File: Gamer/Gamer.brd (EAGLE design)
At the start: 162 x 64 mm, 53 parts, among them J1 AVR_SPI_PRG_6NS, J2 AVR_SPI_PRG_6NS, J3 AVR_SPI_PRG_6NS, J4 AVR_SPI_PRG_6NS

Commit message: gamer - Starting complete redo of Gamer
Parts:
- removed C10, C11, C8, C9: (no value), resistor:C0603
- removed C6: 0.05uF, resistor:C0603
- removed C7: 1uF, resistor:C0603
- removed J4: AVR_SPI_PRG_6NS, SparkFun-Connectors:2X3-NS
- removed PI-HEADER: (no value), pinhead:2X13
- removed R4: Bypass, resistor:R0603
- removed R5, R6, R8, R9: 100K, resistor:R0603
- removed R7: 10, resistor:R0603
- removed U$1, U$13, U$3, U$8: 8X8_LED_MATRIX, ScottSilver:8X8_LED_MATRIX
- removed U$10, U$14, U$4, U$5: ULN2803AFWG, ScottSilver:ULN2803AFWG
- removed U$11, U$15, U$6, U$9: ATTINY48, ScottSilver:ATTINY48
- removed U$12, U$16, U$2, U$7: RES_ARRAY, ScottSilver:RES_ARRAY
- removed U$17, U$18, U$19, U$20, U$21, U$22: 12X12MM_BUTTON, ScottSilver:12X12MM_BUTTON
- removed U$23: MMA8653FCR1, ScottSilver:MMA8653FCR1
- removed U$24, U$26: SMDTACTILE, ScottSilver:SMDTACTILE
- removed U$25: LM386, ScottSilver:LM386
- removed U$29: DF3_1X2, ScottSilver:DF3_1X2
- removed U$30: DF3_1X5, ScottSilver:DF3_1X5
- added A, B, DOWN, LEFT, RIGHT, UP: 12X12MM_BUTTON, Gamer:12X12MM_BUTTON
- added P1: (no value), HeaderConnectorBoard:2X20
- added P2: NONE, LED_Matrix:1X06
- added PROG: NONE, LED_Matrix:2X03
- added SELECT, START: 6X6MM_BUTTON, Gamer:6X6MM_BUTTON
- added U1: MMA8653FCR1, AccelBreakout:MMA8653FCR1
- added U2: ATTINY48, LED_Matrix:ATTINY48
- added U3: ULN2803AFWG, LED_Matrix:ULN2803AFWG
- C1, C2, C3, C4: device resistor:C0603 -> AccelBreakout:C0603
- C5: value (none) -> 1uF; device resistor:153CLV-0605 -> resistor:C0603
- J1: value AVR_SPI_PRG_6NS -> NONE; device SparkFun-Connectors:2X3-NS -> LED_Matrix:1X06
- J2, J3: value AVR_SPI_PRG_6NS -> HEADER-1X8; device SparkFun-Connectors:2X3-NS -> LED_Matrix:HEADER-1X8
- R1, R2: value 1k -> 10K; device resistor:R0603 -> AccelBreakout:R0603
- R3: value Bypass -> 10k
- moved J2 63.8 mm to (54.1, 28.7), turned to 0 degrees
- moved C5 62.6 mm to (63.5, 38.1), turned to 0 degrees
- moved J3 49.6 mm to (56.6, 61.7), turned to 0 degrees
- moved C4 40.1 mm to (115.3, 31.8), turned to 270 degrees
- moved J1 38.0 mm to (77.7, 40.4), turned to 0 degrees
- moved C3 35.0 mm to (112.5, 29.0), turned to 0 degrees
- moved R2 30.7 mm to (112.5, 34.3)
- moved R1 30.6 mm to (108.2, 34.8), turned to 180 degrees
- moved C2 27.7 mm to (109.5, 31.8), turned to 270 degrees
- moved C1 23.4 mm to (107.4, 31.8), turned to 270 degrees
- moved R3 8.46 mm to (56.4, 37.1), flipped to the top, turned to 0 degrees
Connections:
- removed net A: PI-HEADER.7, U$22.3
- removed net AUDIO: U$25.3, U$30.1
- removed net B: PI-HEADER.11, U$21.3
- removed net DOWN: PI-HEADER.18, U$20.2
- removed net LEFT: PI-HEADER.16, U$18.2
- removed net MISO1/MOSI2: J1.1, J2.4, R3.1, U$6.PB3, U$9.PB4
- removed net MISO2/MOSI3: J2.1, J4.4, R4.1, U$15.PB3, U$6.PB4
- removed net MISO3/MOSI4: J3.4, J4.1, U$11.PB3, U$15.PB4
- removed net N$1: U$1.COL0, U$5.O1
- removed net N$10: U$1.ROW6, U$2.2R
- removed net N$100: U$11.PC4, U$12.R2
- removed net N$101: U$11.PC5, U$12.R1
- removed net N$102: U$15.PC7, U$16.R8
- removed net N$103: U$13.COL0, U$14.O1
- removed net N$104: U$13.COL1, U$14.O2
- removed net N$105: U$13.COL2, U$14.O3
- removed net N$106: U$13.COL3, U$14.O4
- removed net N$107: U$13.COL4, U$14.O5
- removed net N$108: U$13.COL5, U$14.O6
- removed net N$109: U$13.COL6, U$14.O7
- removed net N$11: U$1.ROW5, U$2.3R
- removed net N$110: U$13.COL7, U$14.O8
- removed net N$111: U$13.ROW7, U$16.1R
- removed net N$112: U$13.ROW6, U$16.2R
- removed net N$113: U$13.ROW5, U$16.3R
- removed net N$114: U$13.ROW4, U$16.4R
- removed net N$115: U$13.ROW3, U$16.5R
- removed net N$116: U$13.ROW2, U$16.6R
- removed net N$117: U$13.ROW1, U$16.7R
- removed net N$118: U$13.ROW0, U$16.8R
- removed net N$119: U$14.I1, U$15.PD0
- removed net N$12: U$1.ROW4, U$2.4R
- removed net N$120: U$14.I2, U$15.PD1
- removed net N$121: U$14.I3, U$15.PD2
- removed net N$122: U$14.I4, U$15.PD3
- removed net N$123: U$14.I5, U$15.PD4
- removed net N$124: U$14.I6, U$15.PD5
- removed net N$125: U$14.I7, U$15.PD6
- removed net N$126: U$14.I8, U$15.PD7
- removed net N$129: U$15.PC0, U$16.R6
- removed net N$13: U$1.ROW3, U$2.5R
- removed net N$130: U$15.PC1, U$16.R5
- removed net N$131: U$15.PC2, U$16.R4
- removed net N$132: U$15.PC3, U$16.R3
- removed net N$133: U$15.PC4, U$16.R2
- removed net N$134: U$15.PC5, U$16.R1
- removed net N$14: U$1.ROW2, U$2.6R
- removed net N$15: U$1.ROW1, U$2.7R
- removed net N$16: U$1.ROW0, U$2.8R
- removed net N$17: U$5.I1, U$9.PD0
- removed net N$18: U$5.I2, U$9.PD1
- removed net N$19: U$5.I3, U$9.PD2
- removed net N$2: U$1.COL1, U$5.O2
- removed net N$20: U$5.I4, U$9.PD3
- removed net N$21: U$5.I5, U$9.PD4
- removed net N$22: U$5.I6, U$9.PD5
- removed net N$23: U$5.I7, U$9.PD6
- removed net N$24: U$5.I8, U$9.PD7
- removed net N$25: U$2.R7, U$9.PA1
- removed net N$26: U$2.R8, U$9.PC7
- removed net N$27: U$2.R6, U$9.PC0
- removed net N$28: U$2.R5, U$9.PC1
- removed net N$29: U$2.R4, U$9.PC2
- removed net N$3: U$1.COL2, U$5.O3
- removed net N$30: U$2.R3, U$9.PC3
- removed net N$31: U$2.R2, U$9.PC4
- removed net N$32: U$2.R1, U$9.PC5
- removed net N$33: C7.1, U$25.7
- removed net N$35: C5.+, C6.1, U$25.5
- removed net N$36: U$3.COL0, U$4.O1
- removed net N$37: C6.2, R7.2
- removed net N$38: U$3.COL1, U$4.O2
- removed net N$39: U$3.COL2, U$4.O3
- removed net N$4: U$1.COL3, U$5.O4
- removed net N$40: U$3.COL3, U$4.O4
- removed net N$41: U$3.COL4, U$4.O5
- removed net N$42: U$3.COL5, U$4.O6
- removed net N$43: U$3.COL6, U$4.O7
- removed net N$44: U$3.COL7, U$4.O8
- removed net N$45: U$3.ROW7, U$7.1R
- removed net N$46: U$3.ROW6, U$7.2R
- removed net N$47: U$3.ROW5, U$7.3R
- removed net N$48: U$3.ROW4, U$7.4R
- removed net N$49: U$3.ROW3, U$7.5R
- removed net N$5: U$1.COL4, U$5.O5
- removed net N$50: U$3.ROW2, U$7.6R
- removed net N$51: U$3.ROW1, U$7.7R
- removed net N$52: U$3.ROW0, U$7.8R
- removed net N$53: U$4.I1, U$6.PD0
- removed net N$54: U$4.I2, U$6.PD1
- removed net N$55: U$4.I3, U$6.PD2
- removed net N$56: U$4.I4, U$6.PD3
- removed net N$57: U$4.I5, U$6.PD4
- removed net N$58: U$4.I6, U$6.PD5
- removed net N$59: U$4.I7, U$6.PD6
- removed net N$6: U$1.COL5, U$5.O6
- removed net N$60: U$4.I8, U$6.PD7
- removed net N$61: U$6.PA1, U$7.R7
- removed net N$62: U$6.PC7, U$7.R8
- removed net N$63: U$6.PC0, U$7.R6
- removed net N$64: U$6.PC1, U$7.R5
- removed net N$65: U$6.PC2, U$7.R4
- removed net N$66: U$6.PC3, U$7.R3
- removed net N$67: U$6.PC4, U$7.R2
- removed net N$68: U$6.PC5, U$7.R1
- removed net N$69: U$15.PA1, U$16.R7
- removed net N$7: U$1.COL6, U$5.O7
- removed net N$70: U$10.O1, U$8.COL0
- removed net N$71: U$10.O2, U$8.COL1
- removed net N$72: U$10.O3, U$8.COL2
- removed net N$73: U$10.O4, U$8.COL3
- removed net N$74: U$10.O5, U$8.COL4
- removed net N$75: U$10.O6, U$8.COL5
- removed net N$76: U$10.O7, U$8.COL6
- removed net N$77: U$10.O8, U$8.COL7
- removed net N$78: U$12.1R, U$8.ROW7
- removed net N$79: U$12.2R, U$8.ROW6
- removed net N$8: U$1.COL7, U$5.O8
- removed net N$80: U$12.3R, U$8.ROW5
- removed net N$81: U$12.4R, U$8.ROW4
- removed net N$82: U$12.5R, U$8.ROW3
- removed net N$83: U$12.6R, U$8.ROW2
- removed net N$84: U$12.7R, U$8.ROW1
- removed net N$85: U$12.8R, U$8.ROW0
- removed net N$86: U$10.I1, U$11.PD0
- removed net N$87: U$10.I2, U$11.PD1
- removed net N$88: U$10.I3, U$11.PD2
- removed net N$89: U$10.I4, U$11.PD3
- removed net N$9: U$1.ROW7, U$2.1R
- removed net N$90: U$10.I5, U$11.PD4
- removed net N$91: U$10.I6, U$11.PD5
- removed net N$92: U$10.I7, U$11.PD6
- removed net N$93: U$10.I8, U$11.PD7
- removed net N$94: U$11.PA1, U$12.R7
- removed net N$95: U$11.PC7, U$12.R8
- removed net N$96: U$11.PC0, U$12.R6
- removed net N$97: U$11.PC1, U$12.R5
- removed net N$98: U$11.PC2, U$12.R4
- removed net N$99: U$11.PC3, U$12.R3
- removed net RIGHT: PI-HEADER.12, U$19.2
- removed net SELECT: PI-HEADER.15, U$26.1
- removed net SPK: C5.-, U$29.1
- removed net SS: PI-HEADER.24, U$11.PB2, U$15.PB2, U$6.PB2, U$9.PB2
- removed net START: PI-HEADER.13, U$24.1
- removed net UP: PI-HEADER.22, U$17.2
- new net 10/MOSI: P1.19
- new net 11/CLK: P1.23
- new net 12: P1.32
- new net 13: P1.33
- new net 14/TX: P1.8
- new net 15/RX: P1.10
- new net 16: P1.36
- new net 17/RTS: B.3, P1.11
- new net 18: P1.12, RIGHT.2
- new net 19: P1.35
- new net 2/SDA: P1.3
- new net 20: P1.38
- new net 21: P1.40
- new net 22: P1.15, SELECT.2
- new net 23: LEFT.2, P1.16
- new net 24: DOWN.2, P1.18
- new net 25: P1.22, UP.2
- new net 26: P1.37
- new net 27: P1.13, START.2
- new net 3.3V_1: P1.1
- new net 3.3V_2: P1.17
- new net 3/SCL: P1.5
- new net 4: A.3, P1.7
- new net 5: P1.29
- new net 5V_1: P1.4
- new net 5V_2: P1.2
- new net 6: P1.31
- new net 7/CE1: P1.26
- new net 8/CE0: P1.24
- new net 9/MISO: P1.21
- new net COL0: J3.8, U3.O1
- new net COL0_SINK: U2.PD0, U3.I1
- new net COL1: J3.7, U3.O2
- new net COL1_SINK: U2.PD1, U3.I2
- new net COL2: J3.3, U3.O3
- new net COL2_SINK: U2.PD2, U3.I3
- new net COL3: J2.3, U3.O4
- new net COL3_SINK: U2.PD3, U3.I4
- new net COL4: J3.2, U3.O5
- new net COL4_SINK: U2.PD4, U3.I5
- new net COL5: J2.5, U3.O6
- new net COL5_SINK: U2.PD5, U3.I6
- new net COL6: J2.6, U3.O7
- new net COL6_SINK: U2.PD6, U3.I7
- new net COL7: J3.5, U3.O8
- new net COL7_SINK: U2.PD7, U3.I8
- new net CS: J1.4, P2.4, U2.PB2
- new net GND2: P1.25
- new net GND3: P1.20
- new net GND4: P1.14
- new net GND5: P1.6
- new net GND6: P1.39
- new net GND7: P1.34
- new net GND8: P1.30
- new net ID1: P1.27
- new net ID2: P1.28
- new net ROW0: J3.1, U2.PC7
- new net ROW1: J3.6, U2.PA1
- new net ROW2: J2.1, U2.PC0
- new net ROW3: J3.4, U2.PC1
- new net ROW4: J2.8, U2.PC2
- new net ROW5: J2.2, U2.PC3
- new net ROW6: J2.7, U2.PC4
- new net ROW7: J2.4, U2.PC5
- net GND: now also A.1, B.1, C5.2, DOWN.4, LEFT.4, P1.9, P2.6, PROG.2, RIGHT.4, SELECT.4, START.4, U1.6, U1.7, U1.9, U2.AGND, U2.GND, U3.GND, UP.4; no longer C10.2, C11.2, C7.2, C8.2, C9.2, J2.6, J3.6, J4.6, PI-HEADER.6, R7.1, U$10.GND, U$11.AGND, U$11.GND, U$14.GND, U$15.AGND, U$15.GND, U$17.4, U$18.4, U$19.4, U$20.4, U$21.1, U$22.1, U$23.6, U$23.7, U$23.9, U$24.4, U$25.2, U$25.4, U$26.4, U$29.2, U$30.2, U$30.5, U$4.GND, U$5.GND, U$6.AGND, U$6.GND, U$9.AGND, U$9.GND
- net INT1: now also U1.3; no longer PI-HEADER.10, U$23.3
- net INT2: now also U1.5; no longer PI-HEADER.8, U$23.5
- net MISO: now also J1.3, PROG.5, U2.PB4; no longer J3.1, PI-HEADER.21, R3.2, R4.2, U$11.PB4
- net MOSI: now also P2.3, PROG.4, U2.PB3; no longer J1.4, PI-HEADER.19, U$9.PB3
- net N$34: now also U1.4; no longer U$23.4
- net RESET: now also P2.5, PROG.1, R3.2, U2.PC6; no longer J2.5, J3.5, J4.5, R5.1, R6.1, R8.1, R9.1, U$11.PC6, U$15.PC6, U$6.PC6, U$9.PC6
- net SCK: now also J1.2, P2.2, PROG.3, U2.PB5; no longer J1.3, J2.3, J3.3, J4.3, PI-HEADER.23, U$11.PB5, U$15.PB5, U$6.PB5, U$9.PB5
- net SCL: now also R1.1, U1.2; no longer PI-HEADER.5, R2.2, U$23.2
- net SDA: now also R2.1, U1.10; no longer PI-HEADER.3, R1.1, U$23.10
- net VCC: now also C5.1, J1.1, P2.1, PROG.6, R2.2, R3.1, U1.1, U1.8, U2.AVCC, U2.VCC, U3.COMMON; no longer C10.1, C11.1, C8.1, C9.1, J1.2, J2.2, J3.2, J4.2, R2.1, R5.2, R6.2, R8.2, R9.2, U$10.COMMON, U$11.AVCC, U$11.VCC, U$14.COMMON, U$15.AVCC, U$15.VCC, U$23.1, U$23.8, U$25.6, U$30.4, U$4.COMMON, U$5.COMMON, U$6.AVCC, U$6.VCC, U$9.AVCC, U$9.VCC
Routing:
- net GND: track 509.6 -> 0.00 mm, vias 20 -> 0
- net VCC: track 321.8 -> 0.00 mm, vias 12 -> 0
- net SCK: track 266.7 -> 0.00 mm, vias 6 -> 0
- net RESET: track 240.3 -> 0.00 mm, vias 3 -> 0
- net UP: track 199.5 -> 0.00 mm, vias 1 -> 0
- net LEFT: track 169.2 -> 0.00 mm, vias 1 -> 0
- net MISO: track 162.3 -> 0.00 mm, vias 3 -> 0
- net SS: track 156.7 -> 0.00 mm, vias 6 -> 0
- net MOSI: track 152.5 -> 0.00 mm, vias 1 -> 0
- net DOWN: track 151.5 -> 0.00 mm, vias 2 -> 0
- net RIGHT: track 142.0 -> 0.00 mm, vias 4 -> 0
- net START: track 124.9 -> 0.00 mm, vias 3 -> 0
- net SELECT: track 116.5 -> 0.00 mm, vias 3 -> 0
- net MISO3/MOSI4: track 104.7 -> 0.00 mm, vias 2 -> 0
- net MISO1/MOSI2: track 99.5 -> 0.00 mm, vias 3 -> 0
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- removed copper zone on layer 16, net GND
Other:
- board size 162 x 64 mm -> 168.9 x 63.5 mm
- board text removed: "B1"
- board text removed: "B2"
- board text removed: "B3"
- board text removed: "B4"
- board text removed: "B5"
- board text removed: "B6"
- board text removed: "B7"
- board text removed: "B8"
- board text removed: "GND"
- board text removed: "J1"
- board text removed: "J10"
- board text removed: "J11"
- board text removed: "J12"
- board text removed: "J13"
- board text removed: "J14"
- board text removed: "J15"
- board text removed: "J3"
- board text removed: "J4"
- board text removed: "J5"
- board text removed: "J6"
- board text removed: "J7"
- board text removed: "J8"
- board text removed: "J9"
- board text removed: "MISO"
- board text removed: "MOSI"
- board text removed: "RESET"
- board text removed: "SCK"
- board text removed: "U1"
- board text removed: "U2"
- board text removed: "U3"
- board text removed: "U4"
- board text removed: "U5"
- board text removed: "U6"
- board text removed: "U7"
- board text removed: "U8"
- board text removed: "VCC"

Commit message: gamer - Work in progress
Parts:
- removed J1, P2: NONE, LED_Matrix:1X06
- moved SELECT 79.9 mm to (35.6, 57.8), turned to 90 degrees
- moved START 69.0 mm to (27.9, 57.8), turned to 90 degrees
- moved J2 31.0 mm to (56.5, 59.6)
- moved J3 26.1 mm to (56.5, 35.6)
- moved R3 19.7 mm to (69.8, 51.4)
- moved PROG 16.5 mm to (72.6, 57.1), flipped to the bottom
- moved U3 13.6 mm to (53.4, 52.7), turned to 180 degrees
- moved C5 10.9 mm to (69.8, 47.0)
- moved U2 3.70 mm to (61.3, 47.9)
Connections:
- removed net 11/CLK: P1.23
- removed net CS: J1.4, P2.4, U2.PB2
- removed net MISO: J1.3, PROG.5, U2.PB4
- removed net SCK: J1.2, P2.2, PROG.3, U2.PB5
- new net 11/SCLK: P1.23, PROG.3, U2.PB5
- net 8/CE0: now also U2.PB2
- net 9/MISO: now also PROG.5, U2.PB4
- net GND: no longer J1.6, P2.6
- net MOSI: no longer P2.3
- net RESET: no longer J1.5, P2.5
- net VCC: no longer J1.1, P2.1

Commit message: gamer - Duplicated matrices (not laid out)
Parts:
- added C6, C7, C8: 1uF, resistor:C0603
- added J1, J4, J5, J6, J7, J8: HEADER-1X8, LED_Matrix:HEADER-1X8
- added PROG1, PROG2, PROG3: NONE, LED_Matrix:2X03
- added R4, R5, R6: 10k, resistor:R0603
- added U4, U6, U8: ATTINY48, LED_Matrix:ATTINY48
- added U5, U7, U9: ULN2803AFWG, LED_Matrix:ULN2803AFWG
- moved J3 76.2 mm to (10.8, -25.4)
- moved PROG 42.6 mm to (115.2, 58.4), flipped to the top, turned to 270 degrees
- moved J2 24.0 mm to (56.5, 35.6)
- moved P1 2.54 mm to (134.6, 45.7)
- moved U3 1.30 mm to (52.1, 52.7)
- moved A 1.27 mm to (129.5, 16.5)
- moved B 1.27 mm to (143.5, 30.5)
- moved U2 0.54 mm to (61.0, 48.3)
- turned C5 to 90 degrees
- turned R3 to 90 degrees
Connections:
- net COL0_SINK renamed M1_COL0_SINK
- net COL1_SINK renamed M1_COL1_SINK
- net COL2_SINK renamed M1_COL2_SINK
- net COL3_SINK renamed M1_COL3_SINK
- net COL4_SINK renamed M1_COL4_SINK
- net COL5_SINK renamed M1_COL5_SINK
- net COL6_SINK renamed M1_COL6_SINK
- net COL7_SINK renamed M1_COL7_SINK
- net RESET renamed M1_RESET
- removed net COL0: J3.8, U3.O1
- removed net COL1: J3.7, U3.O2
- removed net COL2: J3.3, U3.O3
- removed net COL3: J2.3, U3.O4
- removed net COL4: J3.2, U3.O5
- removed net COL5: J2.5, U3.O6
- removed net COL6: J2.6, U3.O7
- removed net COL7: J3.5, U3.O8
- removed net MOSI: PROG.4, U2.PB3
- removed net ROW0: J3.1, U2.PC7
- removed net ROW1: J3.6, U2.PA1
- removed net ROW2: J2.1, U2.PC0
- removed net ROW3: J3.4, U2.PC1
- removed net ROW4: J2.8, U2.PC2
- removed net ROW5: J2.2, U2.PC3
- removed net ROW6: J2.7, U2.PC4
- removed net ROW7: J2.4, U2.PC5
- new net M1_COL0: J2.8, U3.O1
- new net M1_COL1: J2.7, U3.O2
- new net M1_COL2: J2.3, U3.O3
- new net M1_COL3: J1.3, U3.O4
- new net M1_COL4: J2.2, U3.O5
- new net M1_COL5: J1.5, U3.O6
- new net M1_COL6: J1.6, U3.O7
- new net M1_COL7: J2.5, U3.O8
- new net M1_ROW0: J2.1, U2.PC7
- new net M1_ROW1: J2.6, U2.PA1
- new net M1_ROW2: J1.1, U2.PC0
- new net M1_ROW3: J2.4, U2.PC1
- new net M1_ROW4: J1.8, U2.PC2
- new net M1_ROW5: J1.2, U2.PC3
- new net M1_ROW6: J1.7, U2.PC4
- new net M1_ROW7: J1.4, U2.PC5
- new net M2_COL0: J4.8, U5.O1
- new net M2_COL0_SINK: U4.PD0, U5.I1
- new net M2_COL1: J4.7, U5.O2
- new net M2_COL1_SINK: U4.PD1, U5.I2
- new net M2_COL2: J4.3, U5.O3
- new net M2_COL2_SINK: U4.PD2, U5.I3
- new net M2_COL3: J3.3, U5.O4
- new net M2_COL3_SINK: U4.PD3, U5.I4
- new net M2_COL4: J4.2, U5.O5
- new net M2_COL4_SINK: U4.PD4, U5.I5
- new net M2_COL5: J3.5, U5.O6
- new net M2_COL5_SINK: U4.PD5, U5.I6
- new net M2_COL6: J3.6, U5.O7
- new net M2_COL6_SINK: U4.PD6, U5.I7
- new net M2_COL7: J4.5, U5.O8
- new net M2_COL7_SINK: U4.PD7, U5.I8
- new net M2_RESET: PROG1.1, R4.2, U4.PC6
- new net M2_ROW0: J4.1, U4.PC7
- new net M2_ROW1: J4.6, U4.PA1
- new net M2_ROW2: J3.1, U4.PC0
- new net M2_ROW3: J4.4, U4.PC1
- new net M2_ROW4: J3.8, U4.PC2
- new net M2_ROW5: J3.2, U4.PC3
- new net M2_ROW6: J3.7, U4.PC4
- new net M2_ROW7: J3.4, U4.PC5
- new net M3_COL0: J6.8, U7.O1
- new net M3_COL0_SINK: U6.PD0, U7.I1
- new net M3_COL1: J6.7, U7.O2
- new net M3_COL1_SINK: U6.PD1, U7.I2
- new net M3_COL2: J6.3, U7.O3
- new net M3_COL2_SINK: U6.PD2, U7.I3
- new net M3_COL3: J5.3, U7.O4
- new net M3_COL3_SINK: U6.PD3, U7.I4
- new net M3_COL4: J6.2, U7.O5
- new net M3_COL4_SINK: U6.PD4, U7.I5
- new net M3_COL5: J5.5, U7.O6
- new net M3_COL5_SINK: U6.PD5, U7.I6
- new net M3_COL6: J5.6, U7.O7
- new net M3_COL6_SINK: U6.PD6, U7.I7
- new net M3_COL7: J6.5, U7.O8
- new net M3_COL7_SINK: U6.PD7, U7.I8
- new net M3_RESET: PROG2.1, R5.2, U6.PC6
- new net M3_ROW0: J6.1, U6.PC7
- new net M3_ROW1: J6.6, U6.PA1
- new net M3_ROW2: J5.1, U6.PC0
- new net M3_ROW3: J6.4, U6.PC1
- new net M3_ROW4: J5.8, U6.PC2
- new net M3_ROW5: J5.2, U6.PC3
- new net M3_ROW6: J5.7, U6.PC4
- new net M3_ROW7: J5.4, U6.PC5
- new net M4_COL0: J8.8, U9.O1
- new net M4_COL0_SINK: U8.PD0, U9.I1
- new net M4_COL1: J8.7, U9.O2
- new net M4_COL1_SINK: U8.PD1, U9.I2
- new net M4_COL2: J8.3, U9.O3
- new net M4_COL2_SINK: U8.PD2, U9.I3
- new net M4_COL3: J7.3, U9.O4
- new net M4_COL3_SINK: U8.PD3, U9.I4
- new net M4_COL4: J8.2, U9.O5
- new net M4_COL4_SINK: U8.PD4, U9.I5
- new net M4_COL5: J7.5, U9.O6
- new net M4_COL5_SINK: U8.PD5, U9.I6
- new net M4_COL6: J7.6, U9.O7
- new net M4_COL6_SINK: U8.PD6, U9.I7
- new net M4_COL7: J8.5, U9.O8
- new net M4_COL7_SINK: U8.PD7, U9.I8
- new net M4_RESET: PROG3.1, R6.2, U8.PC6
- new net M4_ROW0: J8.1, U8.PC7
- new net M4_ROW1: J8.6, U8.PA1
- new net M4_ROW2: J7.1, U8.PC0
- new net M4_ROW3: J8.4, U8.PC1
- new net M4_ROW4: J7.8, U8.PC2
- new net M4_ROW5: J7.2, U8.PC3
- new net M4_ROW6: J7.7, U8.PC4
- new net M4_ROW7: J7.4, U8.PC5
- new net MOSI1/MISO2: PROG.4, PROG1.4, PROG2.4, PROG3.4, U2.PB3, U4.PB3, U6.PB3, U8.PB3
- net 11/SCLK: now also PROG1.3, PROG2.3, PROG3.3, U4.PB5, U6.PB5, U8.PB5
- net 8/CE0: now also U4.PB2, U6.PB2, U8.PB2
- net 9/MISO: now also PROG1.5, PROG2.5, PROG3.5, U4.PB4, U6.PB4, U8.PB4
- net GND: now also C6.2, C7.2, C8.2, PROG1.2, PROG2.2, PROG3.2, U4.AGND, U4.GND, U5.GND, U6.AGND, U6.GND, U7.GND, U8.AGND, U8.GND, U9.GND
- net VCC: now also C6.1, C7.1, C8.1, PROG1.6, PROG2.6, PROG3.6, R4.1, R5.1, R6.1, U4.AVCC, U4.VCC, U5.COMMON, U6.AVCC, U6.VCC, U7.COMMON, U8.AVCC, U8.VCC, U9.COMMON

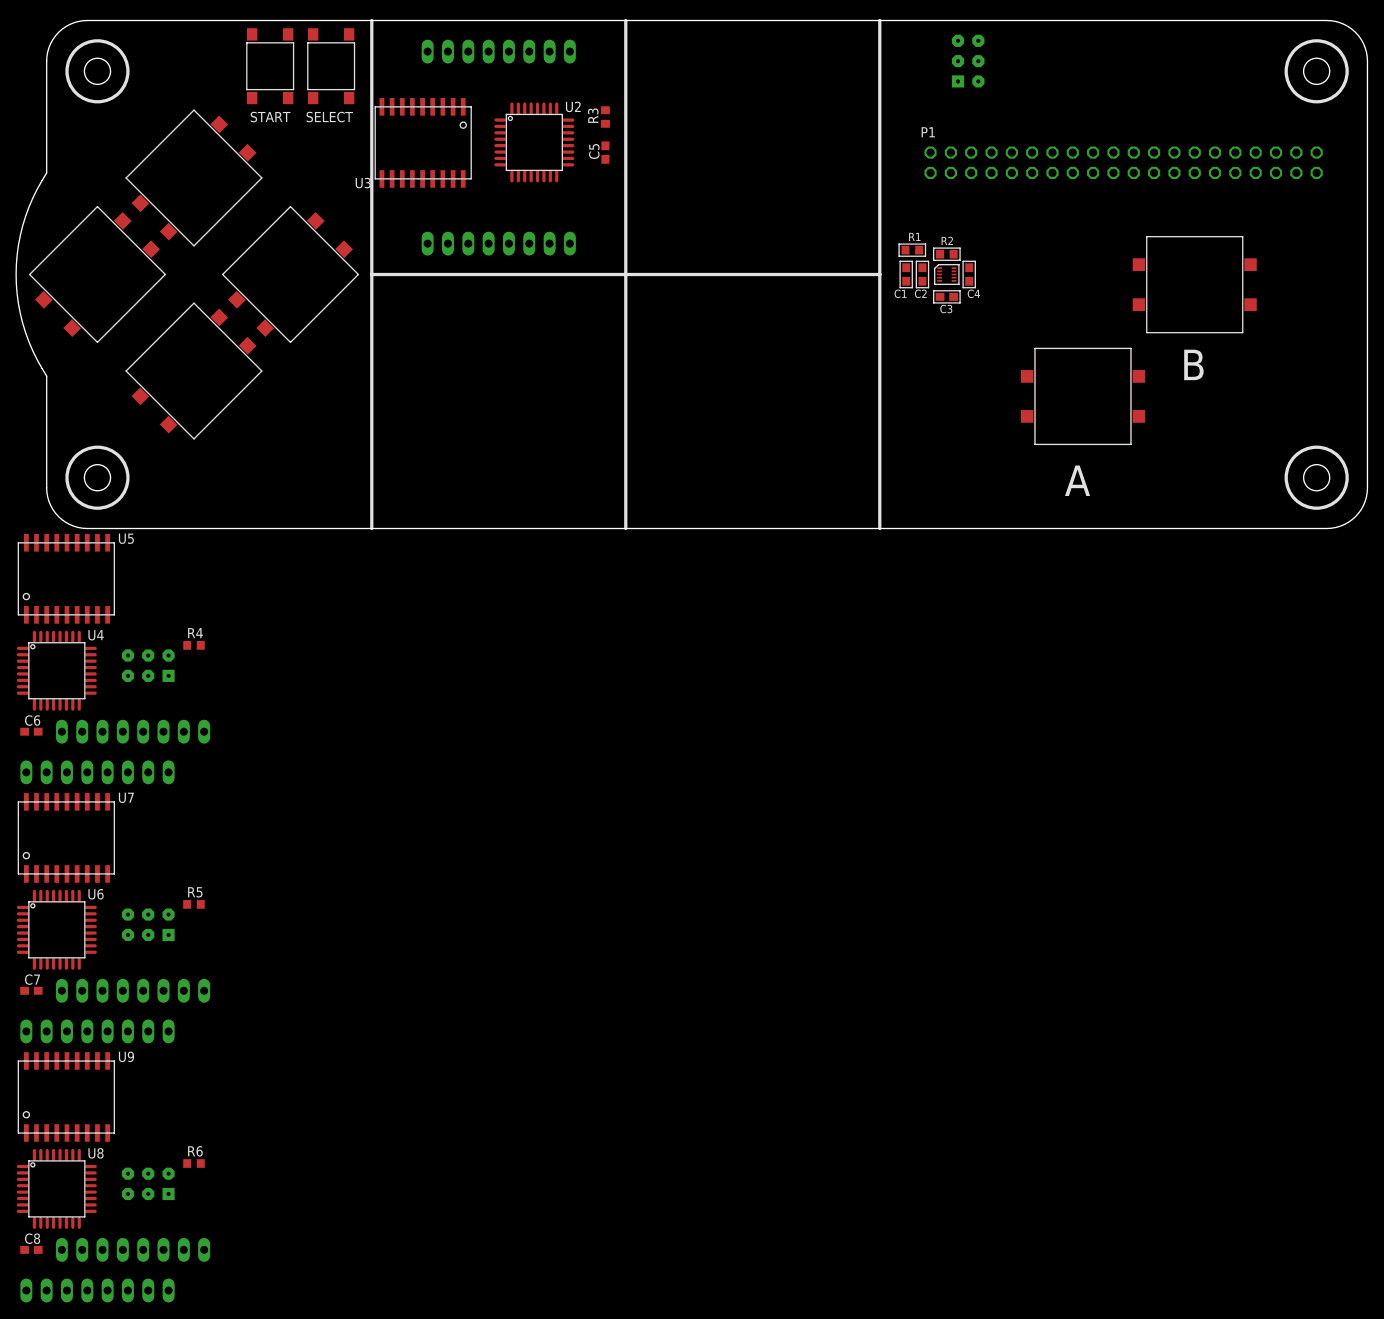
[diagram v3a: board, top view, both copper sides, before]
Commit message: gamer - intial layout of all matrix parts
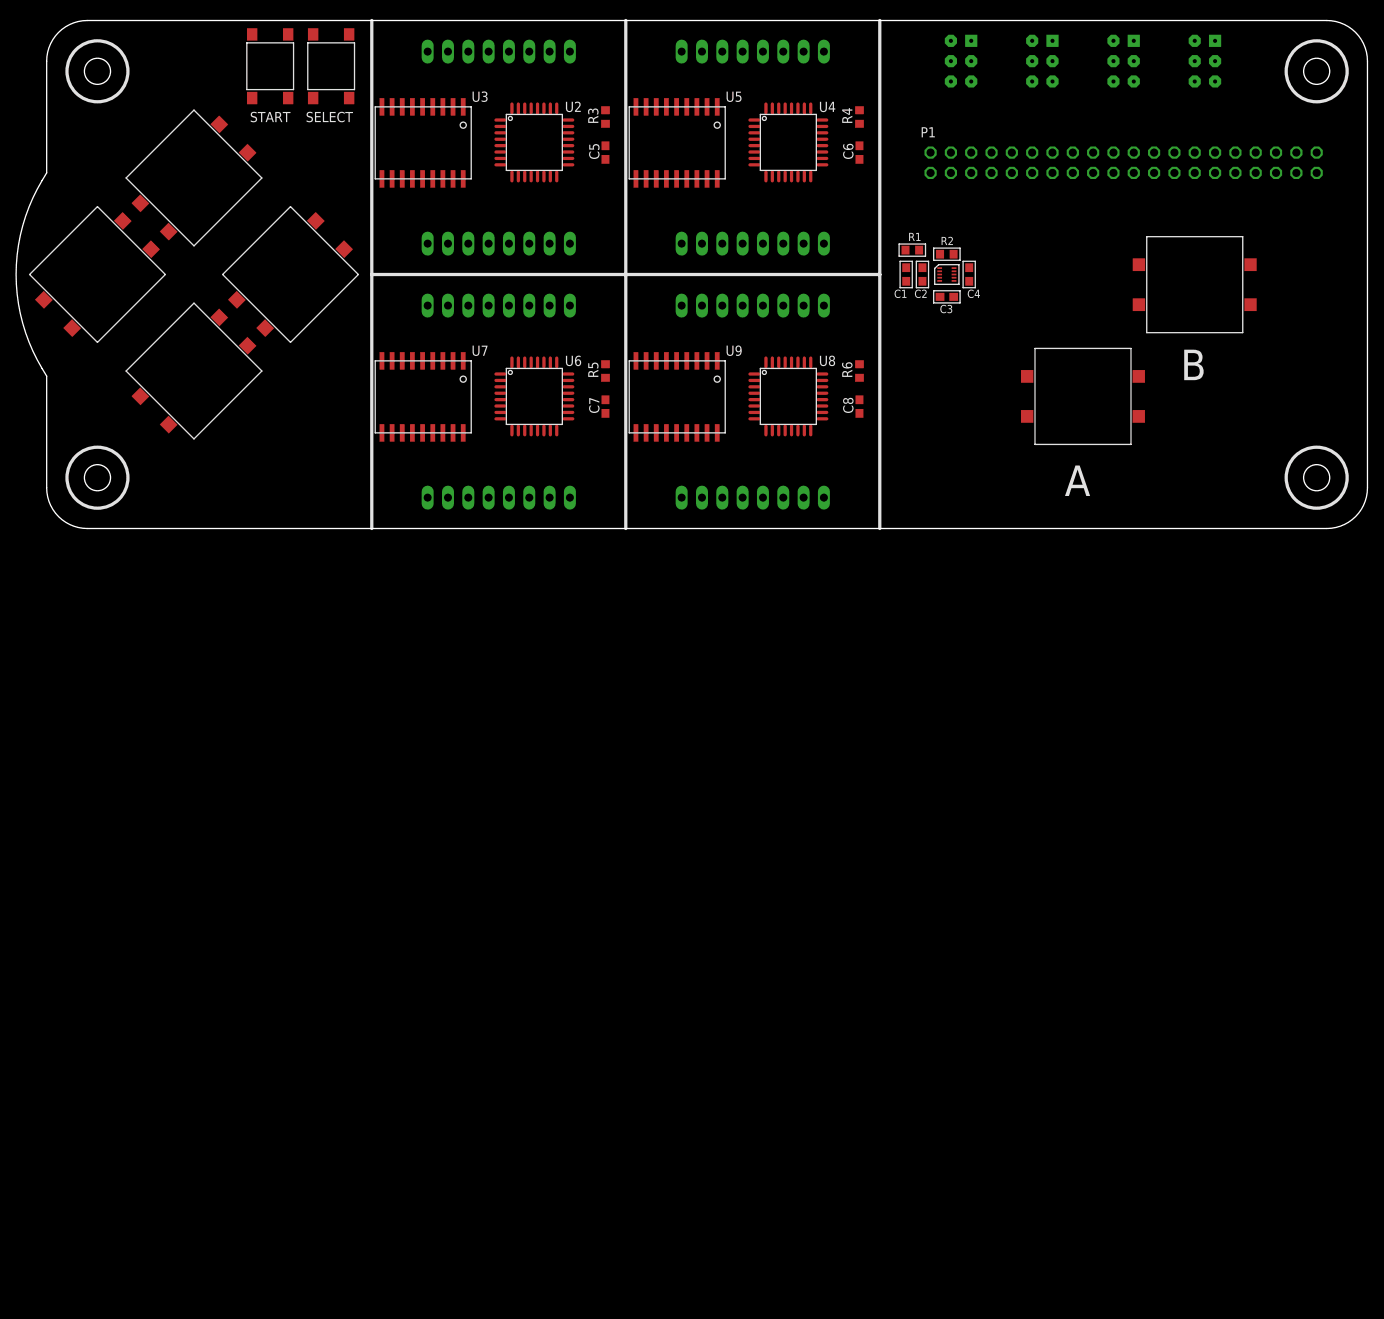
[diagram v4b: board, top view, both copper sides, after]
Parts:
- moved PROG3 192.7 mm to (144.8, 58.4), turned to 90 degrees
- moved PROG2 162.8 mm to (134.6, 58.4), turned to 90 degrees
- moved C8 147.7 mm to (101.6, 15.2), turned to 90 degrees
- moved J7 141.2 mm to (88.3, 27.9)
- moved PROG1 134.9 mm to (124.5, 58.4), turned to 90 degrees
- moved U8 134.8 mm to (92.7, 16.5)
- moved U9 129.5 mm to (83.8, 21.0), turned to 180 degrees
- moved R6 129.4 mm to (101.6, 19.7), turned to 90 degrees
- moved J8 128.6 mm to (88.3, 3.86)
- moved C6 126.3 mm to (101.6, 47.0), turned to 90 degrees
- moved J3 115.0 mm to (88.3, 59.6)
- moved U4 112.8 mm to (92.7, 48.3)
- moved U5 107.2 mm to (83.8, 52.7), turned to 180 degrees
- moved R4 106.2 mm to (101.6, 51.4), turned to 90 degrees
- moved J4 105.3 mm to (88.3, 35.6)
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
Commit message: gamer - rejiggered PROG connectors
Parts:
- removed PROG: NONE, LED_Matrix:2X03
- added PROG4: NONE, Gamer:2X03
- PROG1, PROG2, PROG3: device LED_Matrix:2X03 -> Gamer:2X03
- moved PROG2 10.2 mm to (124.5, 58.4), turned to 270 degrees
- moved PROG1 10.2 mm to (114.3, 58.4), turned to 270 degrees
- moved PROG3 10.2 mm to (134.6, 58.4), turned to 270 degrees
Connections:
- net 11/SCLK: now also PROG4.3; no longer PROG.3
- net 9/MISO: now also PROG1.1, PROG2.1, PROG3.1, PROG4.1; no longer PROG.5, PROG1.5, PROG2.5, PROG3.5
- net GND: now also PROG1.6, PROG2.6, PROG3.6, PROG4.6; no longer PROG.2, PROG1.2, PROG2.2, PROG3.2
- net M1_RESET: now also PROG1.5; no longer PROG.1
- net M2_RESET: now also PROG2.5; no longer PROG1.1
- net M3_RESET: now also PROG3.5; no longer PROG2.1
- net M4_RESET: now also PROG4.5; no longer PROG3.1
- net MOSI1/MISO2: now also PROG4.4; no longer PROG.4
- net VCC: now also PROG1.2, PROG2.2, PROG3.2, PROG4.2; no longer PROG.6, PROG1.6, PROG2.6, PROG3.6
